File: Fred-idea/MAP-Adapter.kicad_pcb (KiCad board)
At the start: 2 copper layers, 19.8 x 11.5 mm, 2 parts, among them U1 SOP8, U6 SSOP8

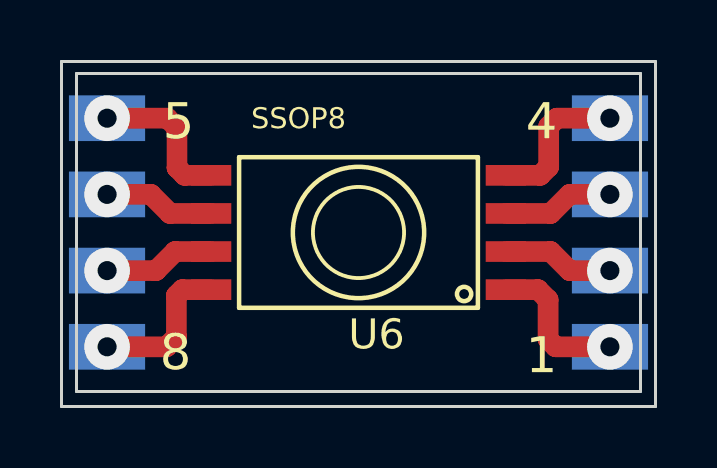
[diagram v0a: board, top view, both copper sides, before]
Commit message: Changed the PCB edge cuts to match the MPX4250A datasheet measurements for the length/width of the component, not including the diameter of the top portion of the sensor.
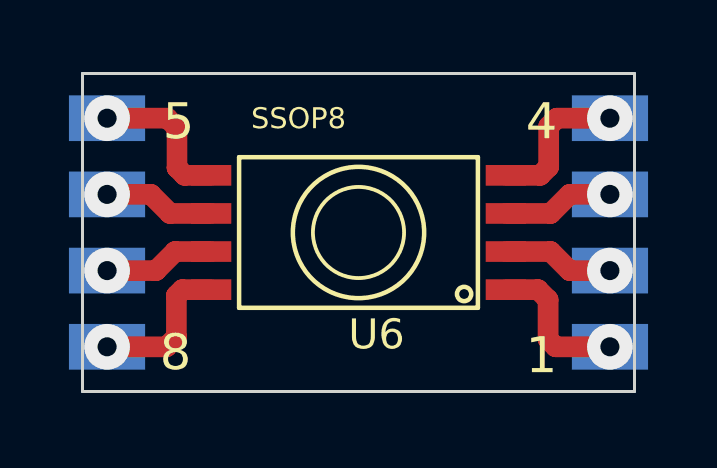
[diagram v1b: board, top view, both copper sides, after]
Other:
- board size 19.8 x 11.5 mm -> 18.4 x 10.6 mm
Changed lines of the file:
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@@
     (area 197.100001 140.650001 234.835715 160.6)
     (thickness 1.6)
-    (drawings 16)
+    (drawings 11)
     (tracks 48)
     (zones 0)
@@
     )
   )
-  (gr_line (start 207 155.8) (end 207 145.2) (angle 90) (layer Edge.Cuts) (width 0.1))
-  (gr_line (start 225.8 155.8) (end 207 155.8) (angle 90) (layer Edge.Cuts) (width 0.1))
-  (gr_line (start 225.8 145.2) (end 225.8 155.8) (angle 90) (layer Edge.Cuts) (width 0.1))
-  (gr_line (start 225.8 145.2) (end 207 145.2) (angle 90) (layer Edge.Cuts) (width 0.1))
+  (dimension 18.4 (width 0.3) (layer Dwgs.User)
+    (gr_text "18.400 mm" (at 216.4 138.150001) (layer Dwgs.User)
+      (effects (font (size 1.5 1.5) (thickness 0.3)))
+    )
+    (feature1 (pts (xy 225.6 144.5) (xy 225.6 136.800001)))
+    (feature2 (pts (xy 207.2 144.5) (xy 207.2 136.800001)))
+    (crossbar (pts (xy 207.2 139.500001) (xy 225.6 139.500001)))
+    (arrow1a (pts (xy 225.6 139.500001) (xy 224.473497 140.086421)))
+    (arrow1b (pts (xy 225.6 139.500001) (xy 224.473497 138.913581)))
+    (arrow2a (pts (xy 207.2 139.500001) (xy 208.326503 140.086421)))
+    (arrow2b (pts (xy 207.2 139.500001) (xy 208.326503 138.913581)))
+  )
+  (gr_line (start 207.2 145.2) (end 225.6 145.2) (angle 90) (layer Edge.Cuts) (width 0.1))
+  (gr_line (start 207.2 155.8) (end 207.2 145.2) (angle 90) (layer Edge.Cuts) (width 0.1))
+  (gr_line (start 207.3 155.8) (end 207.2 155.8) (angle 90) (layer Edge.Cuts) (width 0.1))
+  (gr_line (start 225.6 155.8) (end 207.3 155.8) (angle 90) (layer Edge.Cuts) (width 0.1))
+  (gr_line (start 225.6 145.2) (end 225.6 155.8) (angle 90) (layer Edge.Cuts) (width 0.1))
+  (dimension 10.600472 (width 0.3) (layer Dwgs.User)
+    (gr_text "10.600 mm" (at 233.697544 150.566485 89.45948981) (layer Dwgs.User)
+      (effects (font (size 1.5 1.5) (thickness 0.3)))
+    )
+    (feature1 (pts (xy 226.7 145.2) (xy 235.097484 145.27922)))
+    (feature2 (pts (xy 226.6 155.8) (xy 234.997484 155.87922)))
+    (crossbar (pts (xy 232.297605 155.85375) (xy 232.397605 145.25375)))
+    (arrow1a (pts (xy 232.397605 145.25375) (xy 232.973372 146.385735)))
+    (arrow1b (pts (xy 232.397605 145.25375) (xy 231.800584 146.374671)))
+    (arrow2a (pts (xy 232.297605 155.85375) (xy 232.894626 154.732829)))
+    (arrow2b (pts (xy 232.297605 155.85375) (xy 231.721838 154.721765)))
+  )
   (gr_text 8 (at 210.3 154.5) (layer F.SilkS)
     (effects (font (size 1.2 1.2) (thickness 0.18)))
@@
     (effects (font (size 1.2 1.2) (thickness 0.18)))
   )
-  (dimension 19.8 (width 0.3) (layer Dwgs.User)
-    (gr_text "19.800 mm" (at 216.4 159.249999) (layer Dwgs.User)
-      (effects (font (size 1.5 1.5) (thickness 0.3)))
-    )
-    (feature1 (pts (xy 226.3 156.6) (xy 226.3 160.599999)))
-    (feature2 (pts (xy 206.5 156.6) (xy 206.5 160.599999)))
-    (crossbar (pts (xy 206.5 157.899999) (xy 226.3 157.899999)))
-    (arrow1a (pts (xy 226.3 157.899999) (xy 225.173497 158.486419)))
-    (arrow1b (pts (xy 226.3 157.899999) (xy 225.173497 157.313579)))
-    (arrow2a (pts (xy 206.5 157.899999) (xy 207.626503 158.486419)))
-    (arrow2b (pts (xy 206.5 157.899999) (xy 207.626503 157.313579)))
-  )
-  (dimension 11.5 (width 0.3) (layer Dwgs.User)
-    (gr_text "11.500 mm" (at 203.75 150.55 90) (layer Dwgs.User)
-      (effects (font (size 1.5 1.5) (thickness 0.3)))
-    )
-    (feature1 (pts (xy 206.3 144.8) (xy 202.4 144.8)))
-    (feature2 (pts (xy 206.3 156.3) (xy 202.4 156.3)))
-    (crossbar (pts (xy 205.1 156.3) (xy 205.1 144.8)))
-    (arrow1a (pts (xy 205.1 144.8) (xy 205.68642 145.926503)))
-    (arrow1b (pts (xy 205.1 144.8) (xy 204.51358 145.926503)))
-    (arrow2a (pts (xy 205.1 156.3) (xy 205.68642 155.173497)))
-    (arrow2b (pts (xy 205.1 156.3) (xy 204.51358 155.173497)))
-  )
-  (dimension 11.5 (width 0.3) (layer Eco1.User)
-    (gr_text "0.4528 in" (at 229.15 150.55 90) (layer Eco1.User)
-      (effects (font (size 1.5 1.5) (thickness 0.3)))
-    )
-    (feature1 (pts (xy 226.6 144.8) (xy 230.5 144.8)))
-    (feature2 (pts (xy 226.6 156.3) (xy 230.5 156.3)))
-    (crossbar (pts (xy 227.8 156.3) (xy 227.8 144.8)))
-    (arrow1a (pts (xy 227.8 144.8) (xy 228.38642 145.926503)))
-    (arrow1b (pts (xy 227.8 144.8) (xy 227.21358 145.926503)))
-    (arrow2a (pts (xy 227.8 156.3) (xy 228.38642 155.173497)))
-    (arrow2b (pts (xy 227.8 156.3) (xy 227.21358 155.173497)))
-  )
-  (dimension 19.8 (width 0.3) (layer Eco1.User)
-    (gr_text "0.7795 in" (at 216.4 142.150001) (layer Eco1.User)
-      (effects (font (size 1.5 1.5) (thickness 0.3)))
-    )
-    (feature1 (pts (xy 226.3 144.5) (xy 226.3 140.800001)))
-    (feature2 (pts (xy 206.5 144.5) (xy 206.5 140.800001)))
-    (crossbar (pts (xy 206.5 143.500001) (xy 226.3 143.500001)))
-    (arrow1a (pts (xy 226.3 143.500001) (xy 225.173497 144.086421)))
-    (arrow1b (pts (xy 226.3 143.500001) (xy 225.173497 142.913581)))
-    (arrow2a (pts (xy 206.5 143.500001) (xy 207.626503 144.086421)))
-    (arrow2b (pts (xy 206.5 143.500001) (xy 207.626503 142.913581)))
-  )
-  (gr_line (start 206.5 156.3) (end 226.3 156.3) (angle 90) (layer Edge.Cuts) (width 0.1))
-  (gr_line (start 206.5 144.8) (end 206.5 156.3) (angle 90) (layer Edge.Cuts) (width 0.1))
-  (gr_line (start 226.3 144.8) (end 206.5 144.8) (angle 90) (layer Edge.Cuts) (width 0.1))
-  (gr_line (start 226.3 156.3) (end 226.3 144.8) (angle 90) (layer Edge.Cuts) (width 0.1))
   (segment (start 221.315 151.135) (end 222.805 151.135) (width 0.69) (layer F.Cu) (net 1))
   (segment (start 222.805 151.135) (end 223.44 151.77) (width 0.69) (layer F.Cu) (net 1))
